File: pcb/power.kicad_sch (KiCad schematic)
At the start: 13 parts, among them U5 REG_LDO_3V3_250mA_TI_LP5907MF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, U7 REG_SW_BOOST_TI_TLV61046ADBV

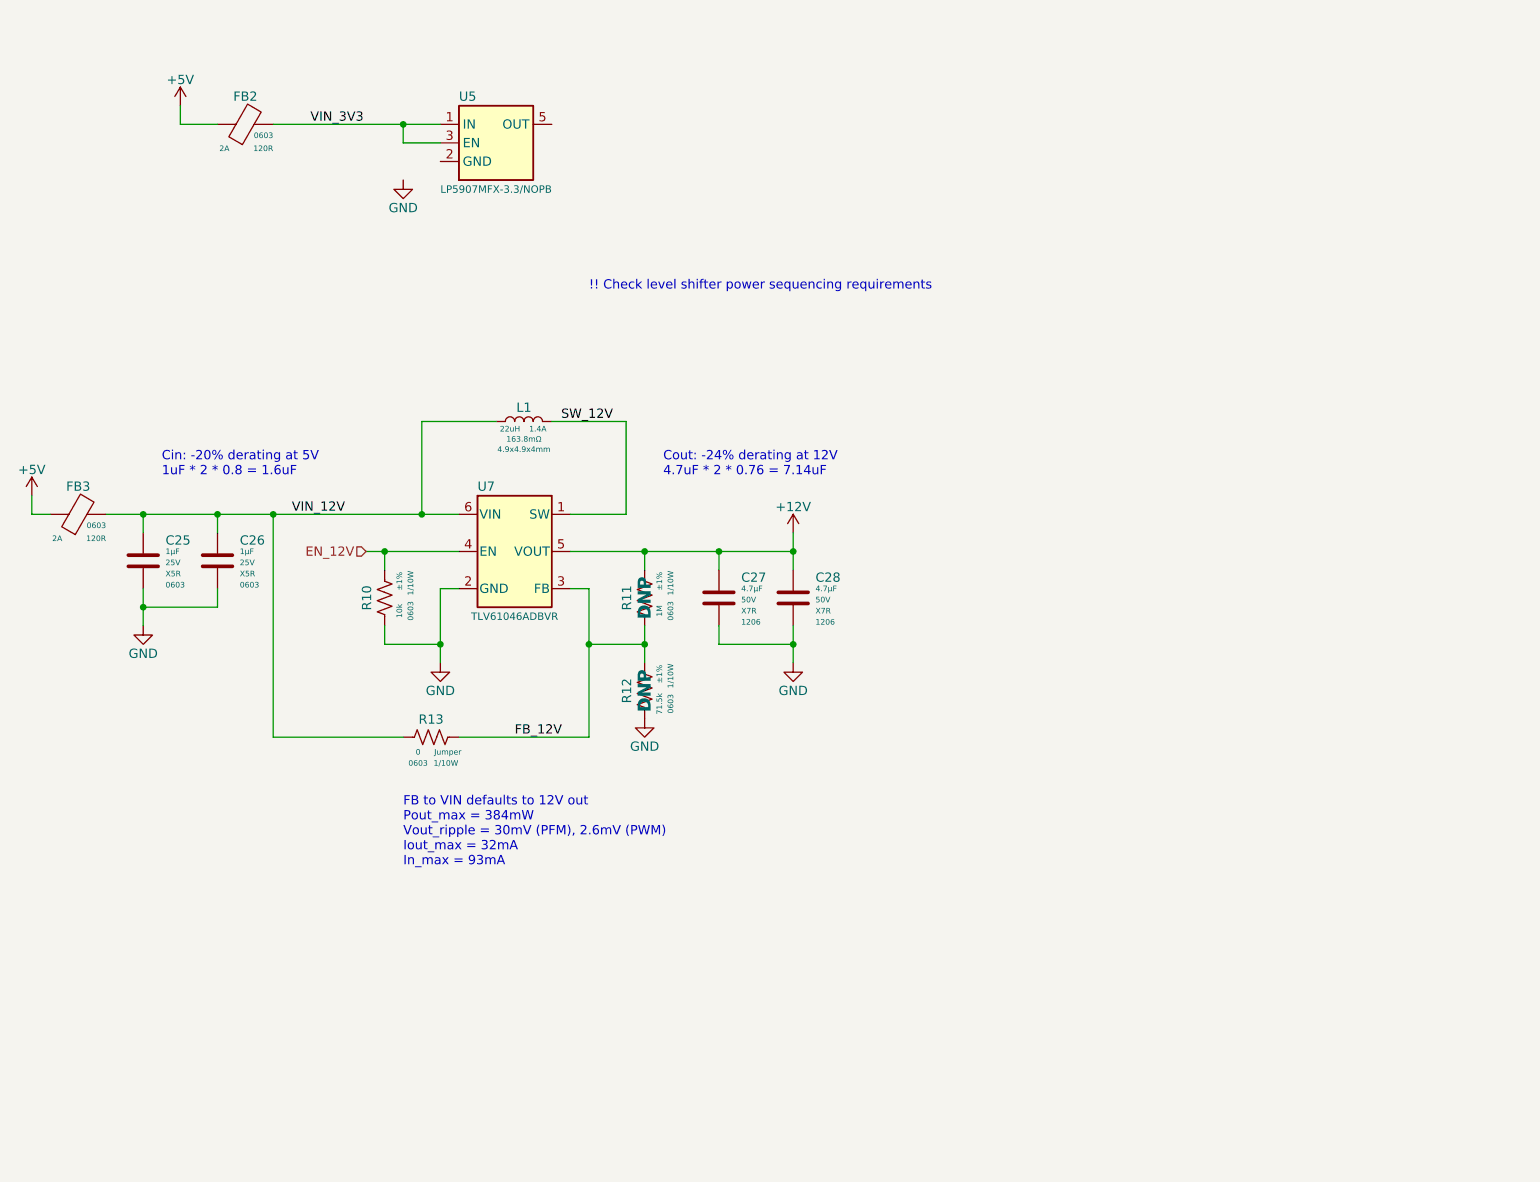
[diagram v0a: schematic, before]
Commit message: Updated caps on 12V Boost, added caps for 3.3V LDO
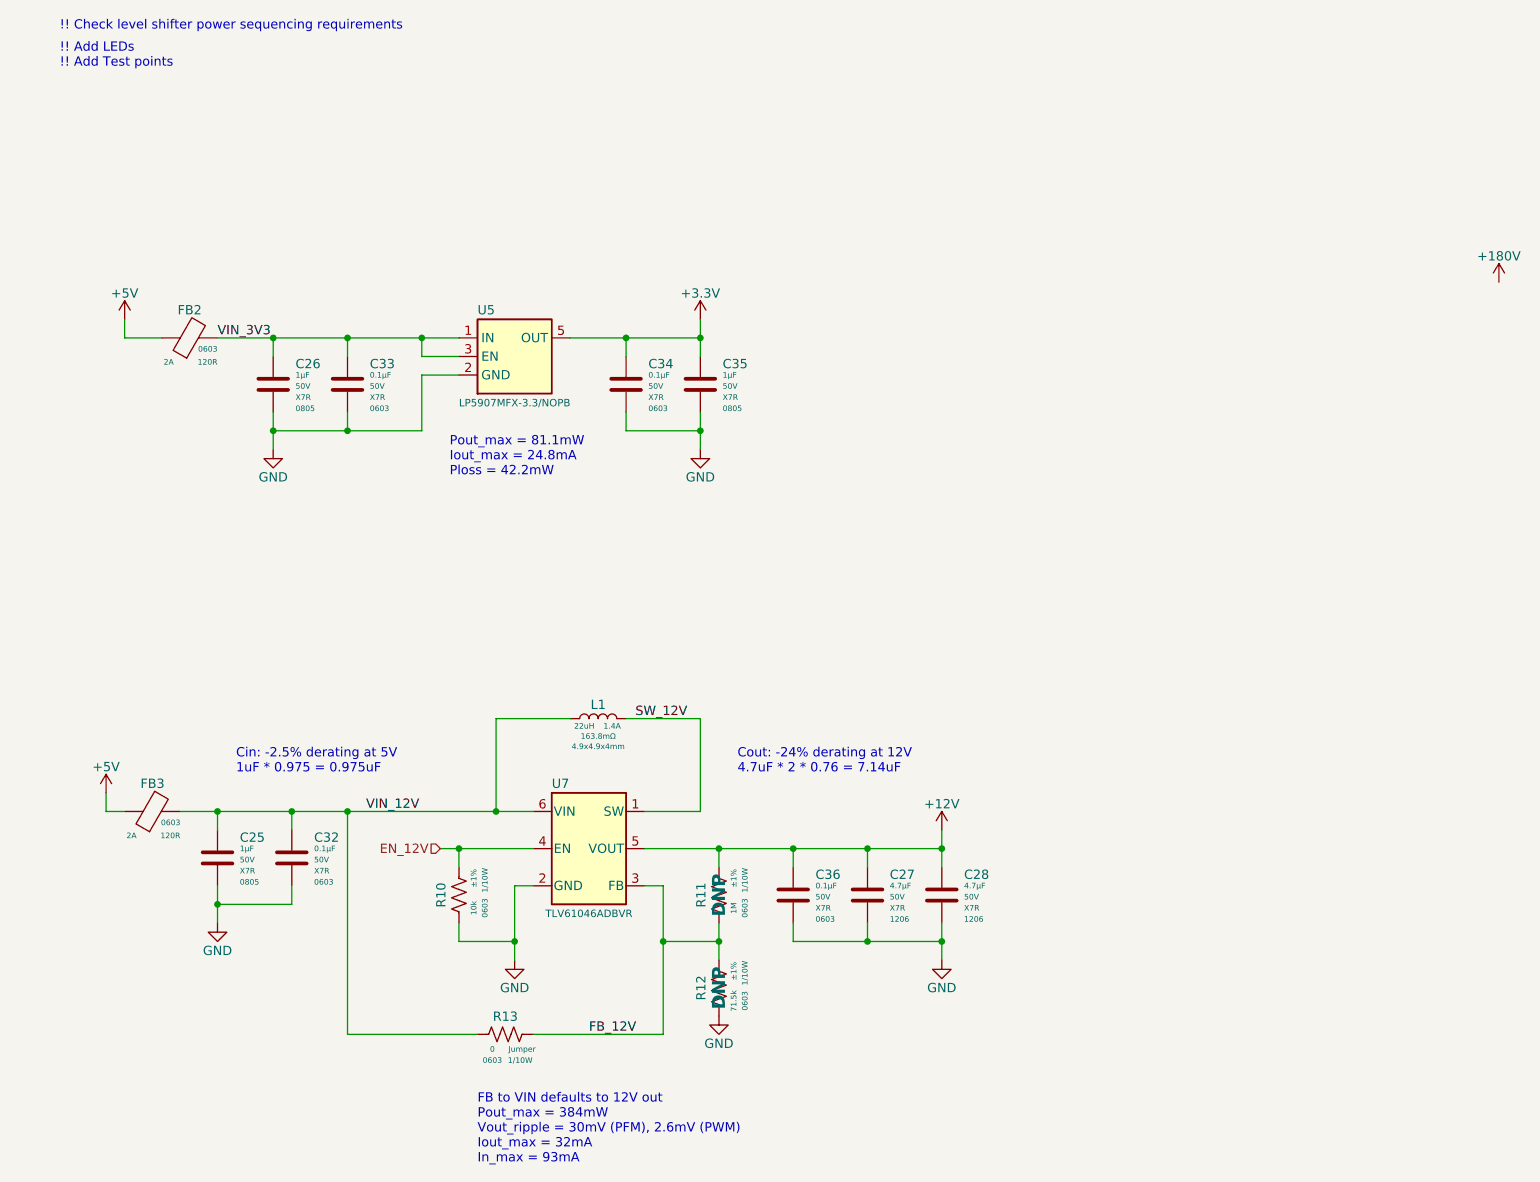
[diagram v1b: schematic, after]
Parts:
- removed C25, C26: CAP_CER_1u_25V_X5R_0603, Capacitor_SMD:C_0603_1608Metric, symbol .arjun:CAP_CER_1u_25V_X5R_0603
- added C25, C26, C35: CAP_CER_1u_50V_X7R_0805, Capacitor_SMD:C_0805_2012Metric, symbol .arjun:CAP_CER_1u_50V_X7R_0805
- added C32, C33, C34, C36: CAP_CER_0u1_50V_X7R_0603, Capacitor_SMD:C_0603_1608Metric, symbol arjun_symbols:CAP_CER_0u1_50V_X7R_0603
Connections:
- net +12V: now also C36.1
- net GND: now also U5.2 (GND), C25.2, C26.2, C32.2, C33.2, C34.2, C35.2, C36.2
- net VIN_12V: now also C25.1, C32.1
- net VIN_3V3: now also C26.1, C33.1
- net +3.3V: now reaches U5.5 (OUT)
- net +3.3V: now also C34.1, C35.1
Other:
- note added: "!! Add LEDs !! Add Test points"
- note added: "Cin: -2.5% derating at 5V 1uF * 0.975 = 0.975uF"
- note added: "Pout_max = 81.1mW Iout_max = 24.8mA Ploss = 42.2mW"
- note removed: "Cin: -20% derating at 5V 1uF * 2 * 0.8 = 1.6uF"
- moved on the sheet: C27, C28, FB2, FB3, L1, R10, R11, R12, R13, U5, U7

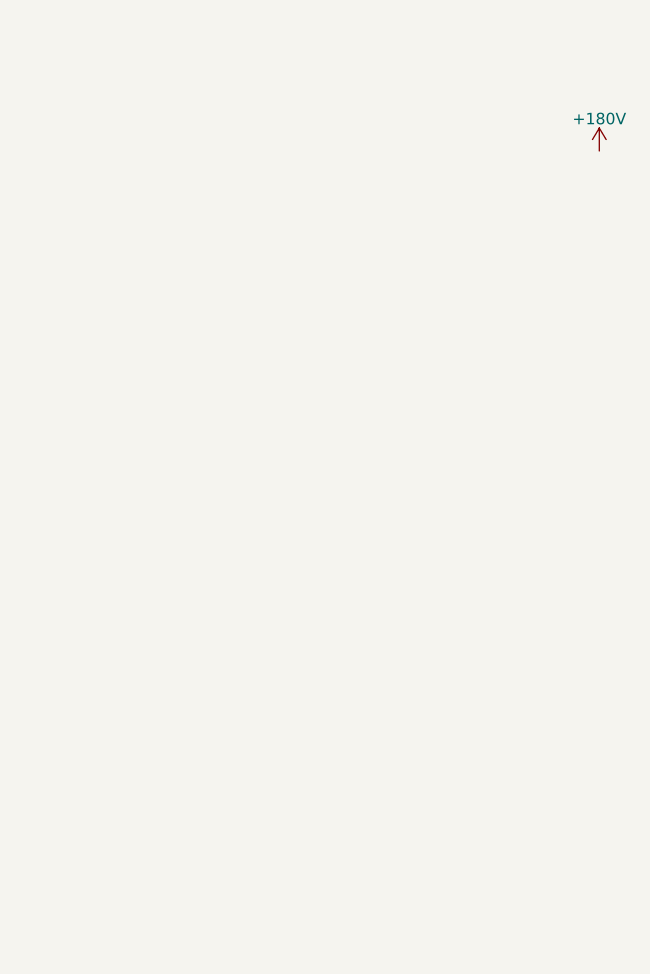
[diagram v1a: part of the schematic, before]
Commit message: Started adding 180V boost components
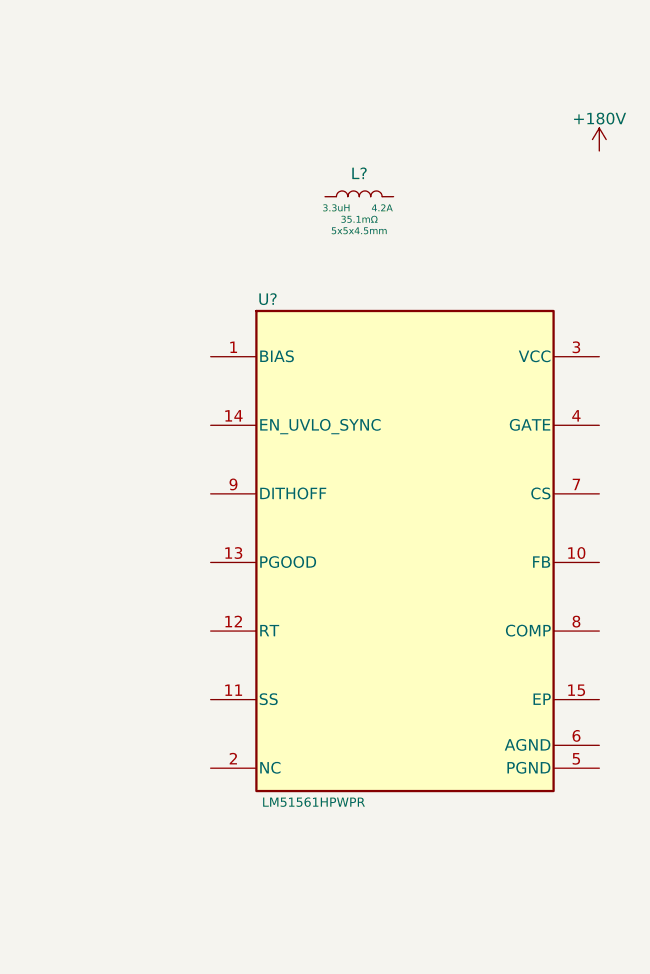
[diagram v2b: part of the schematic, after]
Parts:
- added L?: IND_3u3_4A2_35m1R_5x5x4r5, arjun_footprints:IND_VLS5045EX-3R3N, symbol .arjun:IND_3u3_4A2_35m1R_5x5x4r5
- added U?: REG_SW_BOOST_TI_LM51561HPWPR, arjun_footprints:PWP0014H-MFG, symbol .arjun:REG_SW_BOOST_TI_LM51561HPWPR
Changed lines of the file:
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@@
   (symbol (lib_id "arjun_symbols:+180V") (at 218.44 54.61 0) (unit 1)
     (in_bom yes) (on_board yes)
-    (property "Reference" "#PWR?" (id 0) (at 218.44 58.42 0)
+    (property "Reference" "#PWR0106" (id 0) (at 218.44 58.42 0)
       (effects (font (size 1.27 1.27)) hide)
     )
@@
     )
     (pin "1")
+  )
+  (symbol (lib_id ".arjun:REG_SW_BOOST_TI_LM51561HPWPR") (at 175.26 77.47 0) (unit 1)
+    (in_bom yes) (on_board yes)
+    (property "Reference" "U?" (id 0) (at 181.61 71.12 0))
+    (property "Value" "REG_SW_BOOST_TI_LM51561HPWPR" (id 1) (at 234.95 72.39 0)
+      (effects (font (size 1.27 1.27)) (justify left) hide)
+    )
+    (property "Footprint" "arjun_footprints:PWP0014H-MFG" (id 2) (at 212.09 76.2 0)
+      (effects (font (size 1.27 1.27) italic) (justify left) hide)
+    )
+    (property "Datasheet" "https://www.ti.com/general/docs/suppproductinfo.tsp?distId=10&gotoUrl=http%3A%2F%2Fwww.ti.com%2Flit%2Fgpn%2FLM5156H" (id 3) (at 234.95 83.82 0)
+      (effects (font (size 1.27 1.27)) (justify left) hide)
+    )
+    (property "Manufacturer" "Texas Instruments" (id 4) (at 234.95 81.28 0)
+      (effects (font (size 1.27 1.27)) (justify left) hide)
+    )
+    (property "ManufacturerPN" "LM51561HPWPR" (id 5) (at 186.69 127 0)
+      (effects (font (size 1.016 1.016)))
+    )
+    (property "Vendor" "Digi-Key" (id 6) (at 234.95 76.2 0)
+      (effects (font (size 1.27 1.27)) (justify left) hide)
+    )
+    (property "VendorPN" "296-LM51561HPWPRCT-ND" (id 7) (at 234.95 78.74 0)
+      (effects (font (size 1.27 1.27)) (justify left) hide)
+    )
+    (pin "1")
+    (pin "10")
+    (pin "11")
+    (pin "12")
+    (pin "13")
+    (pin "14")
+    (pin "15")
+    (pin "2")
+    (pin "3")
+    (pin "4")
+    (pin "5")
+    (pin "6")
+    (pin "7")
+    (pin "8")
+    (pin "9")
   )
   (symbol (lib_id "power:GND") (at 109.22 77.47 0) (unit 1)
@@
     (pin "1")
   )
+  (symbol (lib_name "IND_3u3_4A2_35m1R_5x5x4r5_1") (lib_id ".arjun:IND_3u3_4A2_35m1R_5x5x4r5") (at 187.96 59.69 0) (unit 1)
+    (in_bom yes) (on_board yes)
+    (property "Reference" "L?" (id 0) (at 191.77 57.15 0))
+    (property "Value" "IND_3u3_4A2_35m1R_5x5x4r5" (id 1) (at 205.105 54.61 0)
+      (effects (font (size 1.27 1.27)) (justify left) hide)
+    )
+    (property "Footprint" "arjun_footprints:IND_VLS5045EX-3R3N" (id 2) (at 205.74 52.07 0)
+      (effects (font (size 1.27 1.27)) (justify left) hide)
+    )
+    (property "Datasheet" "https://product.tdk.com/system/files/dam/doc/product/inductor/inductor/smd/catalog/inductor_commercial_power_vls5045ex_en.pdf" (id 3) (at 205.105 57.15 0)
+      (effects (font (size 1.27 1.27)) (justify left) hide)
+    )
+    (property "Vendor" "Digi-Key" (id 4) (at 205.105 60.96 0)
+      (effects (font (size 1.27 1.27)) (justify left) hide)
+    )
+    (property "VendorPN" "445-174398-1-ND" (id 5) (at 205.105 63.5 0)
+      (effects (font (size 1.27 1.27)) (justify left) hide)
+    )
+    (property "Manufacturer" "TDK Corporation" (id 6) (at 205.105 66.04 0)
+      (effects (font (size 1.27 1.27)) (justify left) hide)
+    )
+    (property "ManufacturerPN" "VLS5045EX-3R3N" (id 7) (at 205.105 68.58 0)
+      (effects (font (size 1.27 1.27)) (justify left) hide)
+    )
+    (property "Inductance" "3.3uH" (id 8) (at 189.23 60.96 0)
+      (effects (font (size 0.762 0.762)))
+    )
+    (property "Irated" "4.2A" (id 9) (at 194.31 60.96 0)
+      (effects (font (size 0.762 0.762)))
+    )
+    (property "DCR" "35.1mΩ" (id 10) (at 191.77 62.23 0)
+      (effects (font (size 0.762 0.762)))
+    )
+    (property "Dimensions" "5x5x4.5mm" (id 11) (at 191.77 63.5 0)
+      (effects (font (size 0.762 0.762)))
+    )
+    (pin "1")
+    (pin "2")
+  )
   (symbol (lib_id ".arjun:IND_22u_1A4_163m8R_4r9x4r9x4") (at 91.44 114.3 0) (unit 1)
